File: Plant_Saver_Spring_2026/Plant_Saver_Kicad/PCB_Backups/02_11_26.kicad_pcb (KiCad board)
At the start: 2 copper layers, 110 parts, among them J10 DM3D-SF, J11 Test, J2 SBH11-PBPC-D05-ST-BK, J3 SM04B-SRSS-TB, J5 Conn_01x02_Pin, J6 Conn_01x06_Socket, J7 S3B-PH-K-S, J8 54-00284, J9 1.25mm, Q1 G09P02L, Q10 G09P02L, Q11 ISP12DP06NMXTSA1, Q12 G09P02L, Q2 G09P02L, Q3 ISP12DP06NMXTSA1, Q4 G09P02L, Q5 G09P02L, Q6 G09P02L, Q7 G09P02L, Q8 G09P02L, Q9 G09P02L, SW1 Reset, SW2 25336NA, SW3 Boot, SW4 SA72SB0, U1 CDBA140SL-HF, U10 DW03C, U11 CDBA140SL-HF, U12 LP38511TJ-ADJ/NOPB, U13 MCP73833-xxx-UN, U14 MCP6234, U15 MCP73833-xxx-UN, U16 MCP6547T_I_MS, U2 CDBA140SL-HF, U3 CDBA140SL-HF, U4 CDBA140SL-HF, U5 ESP32-WROOM-32E-N16, U9 CDBA140SL-HF

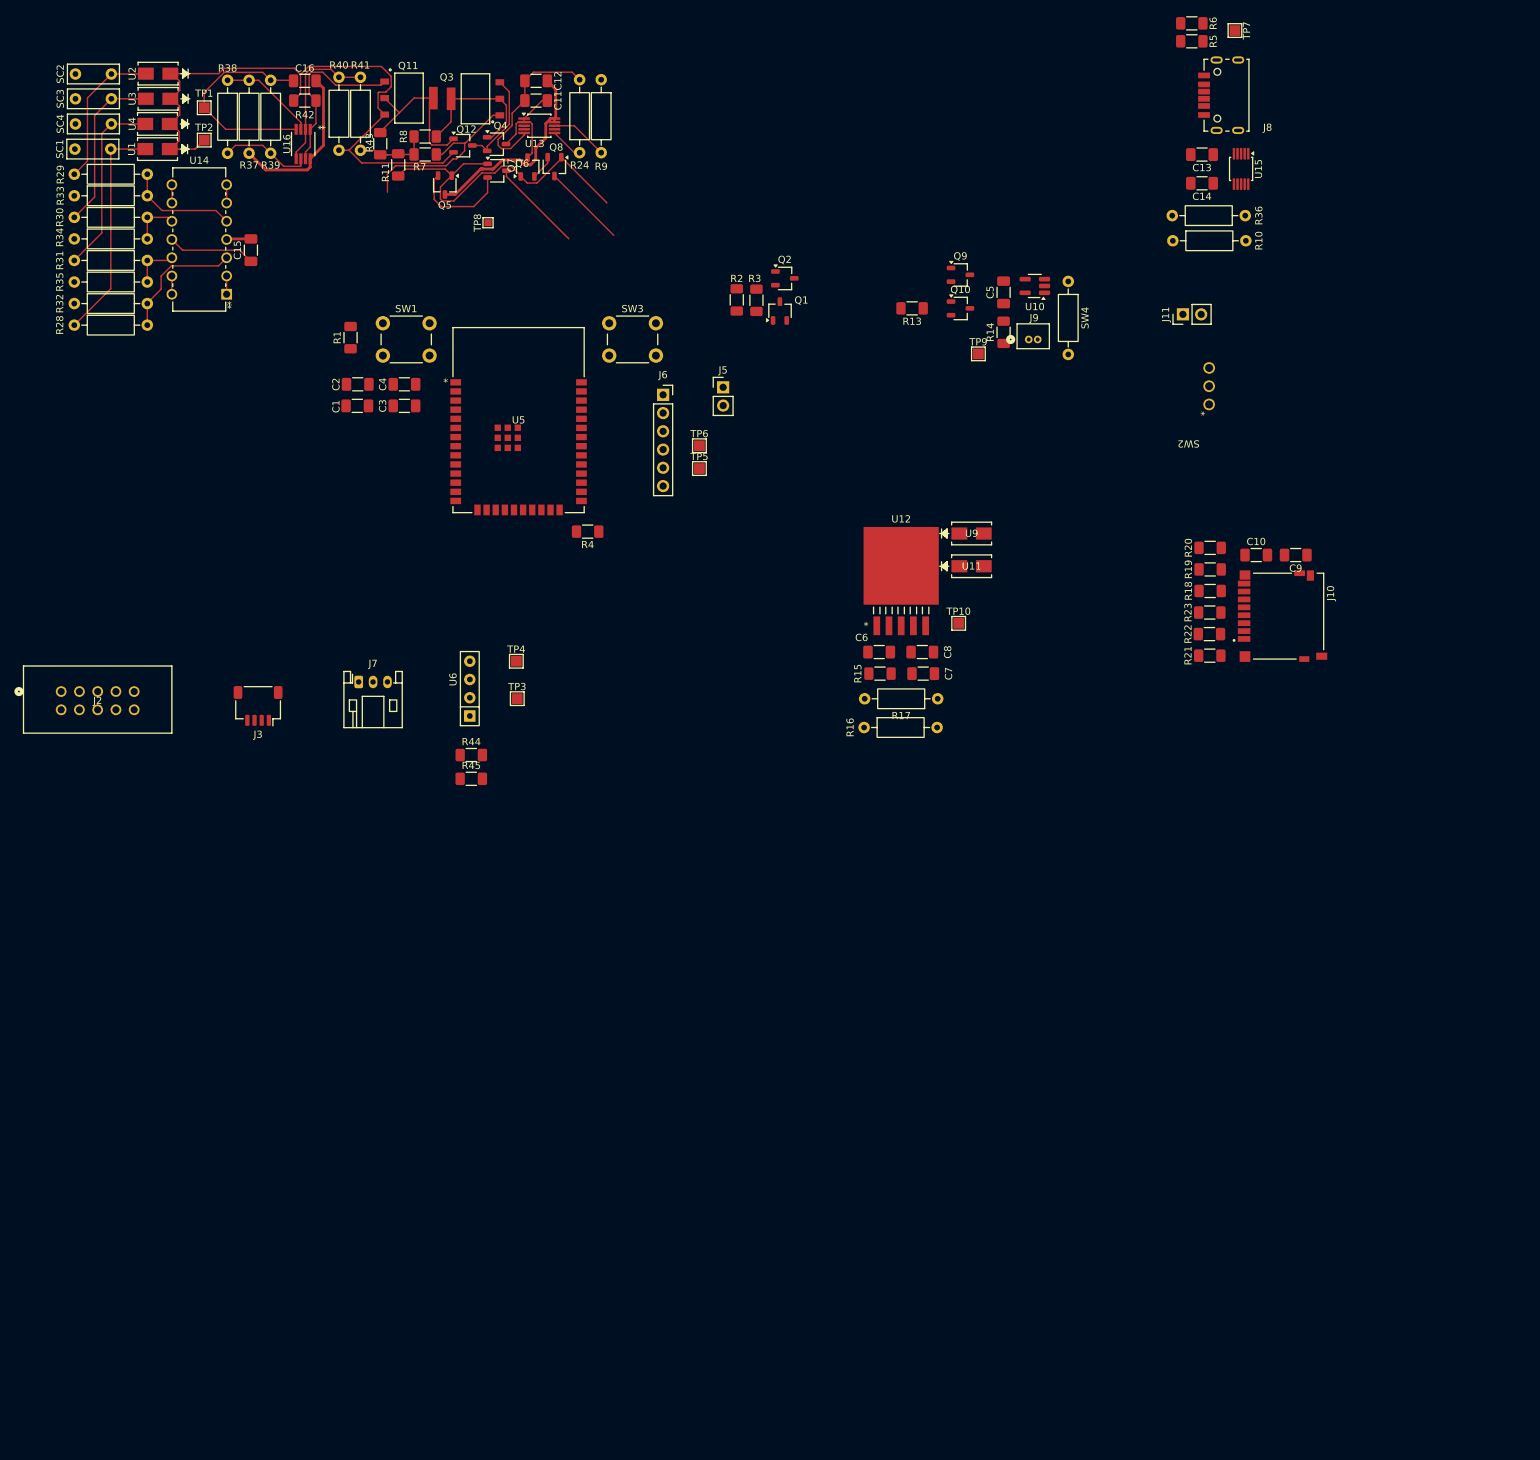
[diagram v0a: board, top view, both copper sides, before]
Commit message: Re-routed to free trapped lines
Repositioned & re-routed to free some nets and get parts within board edge (sorry Noah)
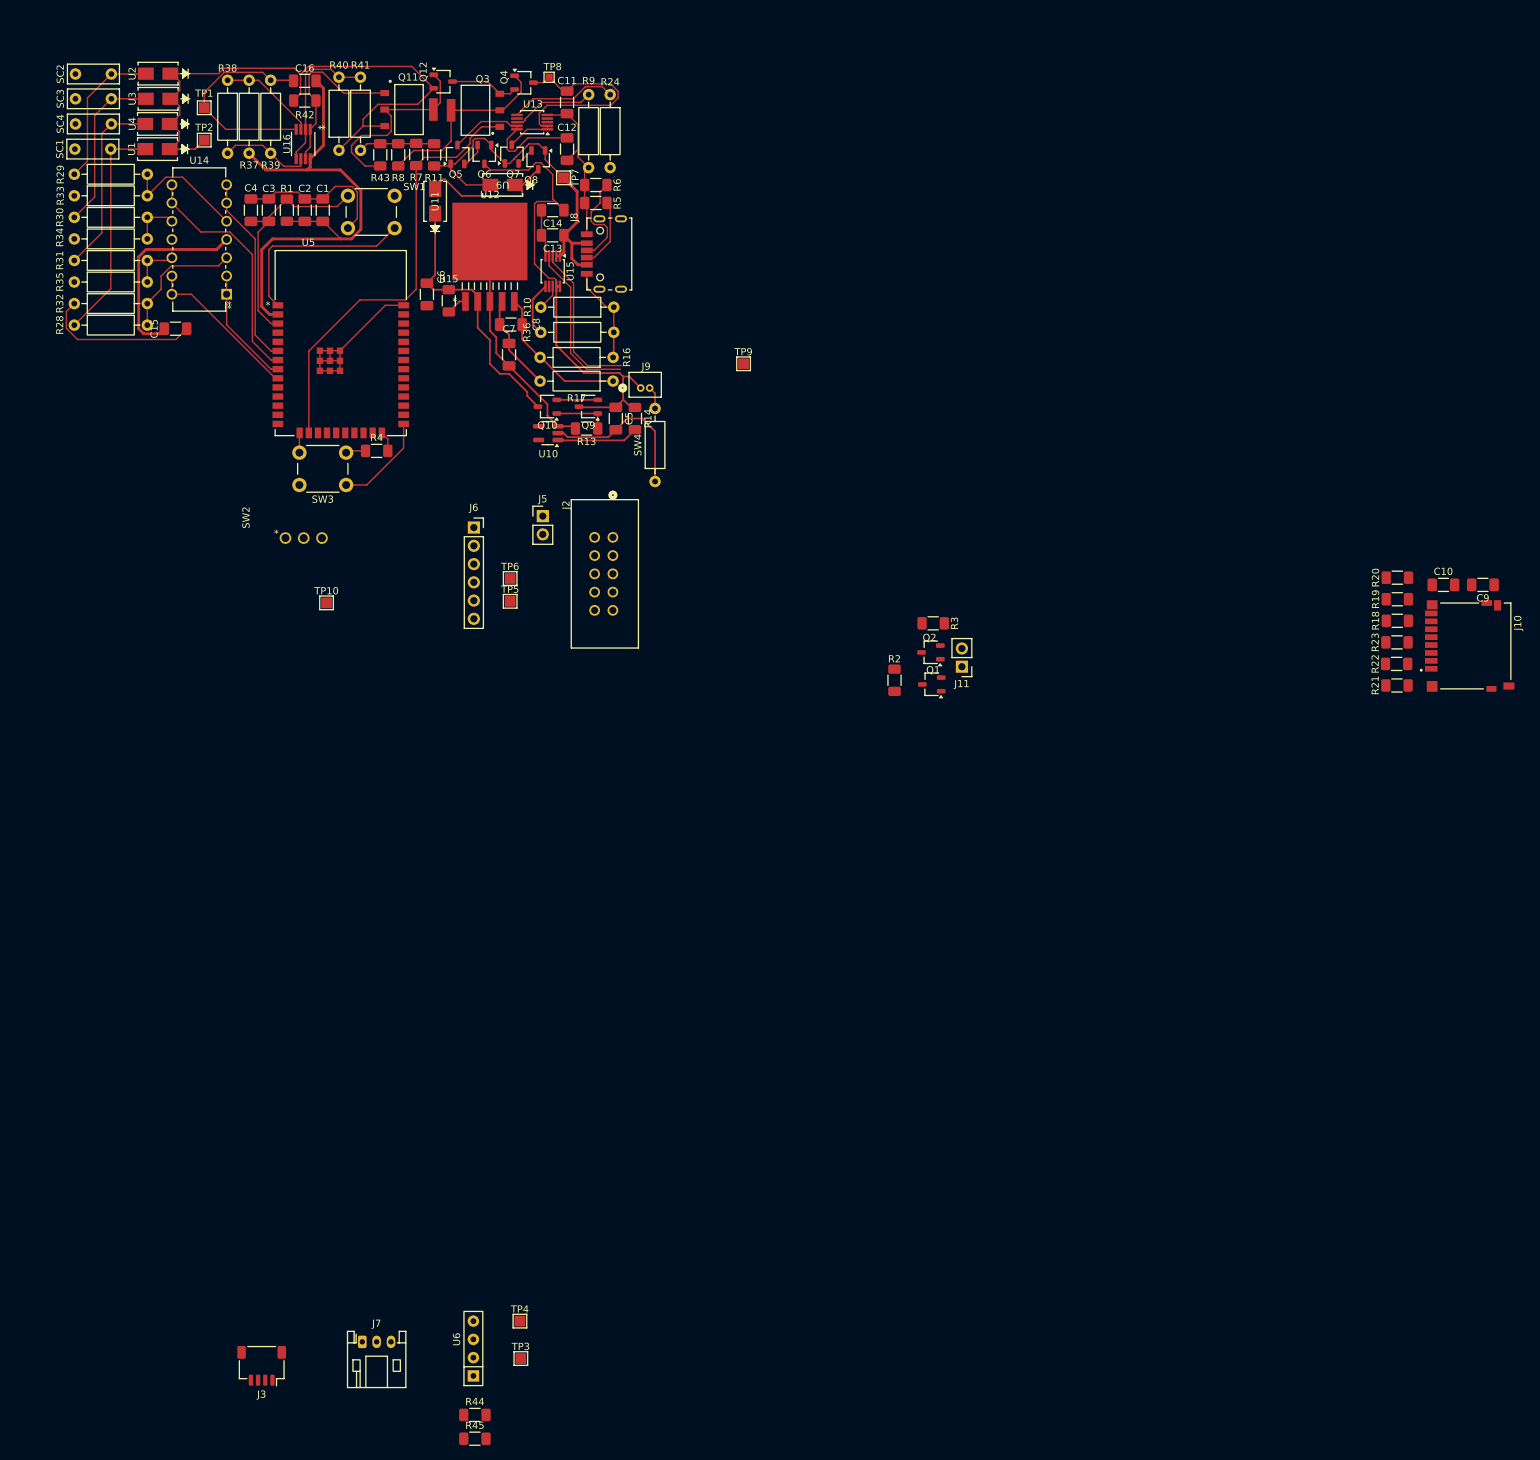
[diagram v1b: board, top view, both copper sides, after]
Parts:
- moved SW2 129.9 mm to (59.3, 135.6), turned to 0 degrees
- moved R36 99.4 mm to (94.8, 107.0), turned to 0 degrees
- moved U15 96.9 mm to (96.5, 98.5)
- moved TP7 95.7 mm to (98.0, 85.5)
- moved TP4 91.8 mm to (91.9, 244.6)
- moved J3 91.8 mm to (56.0, 250.8)
- moved J7 91.8 mm to (70.0, 247.5)
- moved R44 91.8 mm to (85.7, 257.7)
- moved R45 91.8 mm to (85.7, 261.0)
- moved TP3 91.8 mm to (92.1, 249.8)
- moved U6 91.8 mm to (85.5, 252.2)
- moved C13 91.1 mm to (96.5, 93.5)
- moved C14 90.4 mm to (96.5, 90.0)
- moved U11 90.3 mm to (80.1, 88.8), turned to 90 degrees
- moved J8 88.7 mm to (103.1, 96.1)
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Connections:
- U5 pad 6: V_Solar1 -> V_Solar2
- U5 pad 7: V_Solar2 -> V_Solar3
- U5 pad 8: V_Solar3 -> V_Solar1
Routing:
- net GND: track 76.9 -> 220.5 mm
- net /Power_And_Charging/MCP73833_USB/Vbat: track 13.1 -> 69.7 mm
- net Vbus: track 22.8 -> 71.0 mm
- net /Power_And_Charging/Linear_Regulator/Vin: track 0.00 -> 37.6 mm
- net Solar_Chg_EN: track 26.8 -> 61.4 mm
- net Net-(U5-EN): track 0.00 -> 32.7 mm
- net V_Solar3: track 2.54 -> 33.4 mm
- net V_Solar2: track 2.54 -> 26.6 mm
- net Vperiph: track 3.92 -> 27.5 mm
- net STAT2: track 0.00 -> 22.6 mm
- net Net-(U10-GND): track 0.00 -> 22.5 mm
- net STAT1: track 0.00 -> 22.0 mm
- net Net-(U12-ADJ): track 0.00 -> 20.8 mm
- net /Power_And_Charging/MCP73833_Solar/Vin: track 15.5 -> 35.6 mm
- net V_Solar4: track 2.54 -> 22.1 mm
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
